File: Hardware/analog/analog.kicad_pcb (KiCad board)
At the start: 4 copper layers, 128 x 182 mm, 117 parts, among them J201 Würth 74651194R, J202 Würth 74651194R, J301 Conn_02x10_Odd_Even, J501 Conn_01x01, J502 Conn_01x01, M501 Fan_4pin, Q201 IXTH80N075L2, Q501 MMBT3904, U201 ADA4522-2, U202 LM431SC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

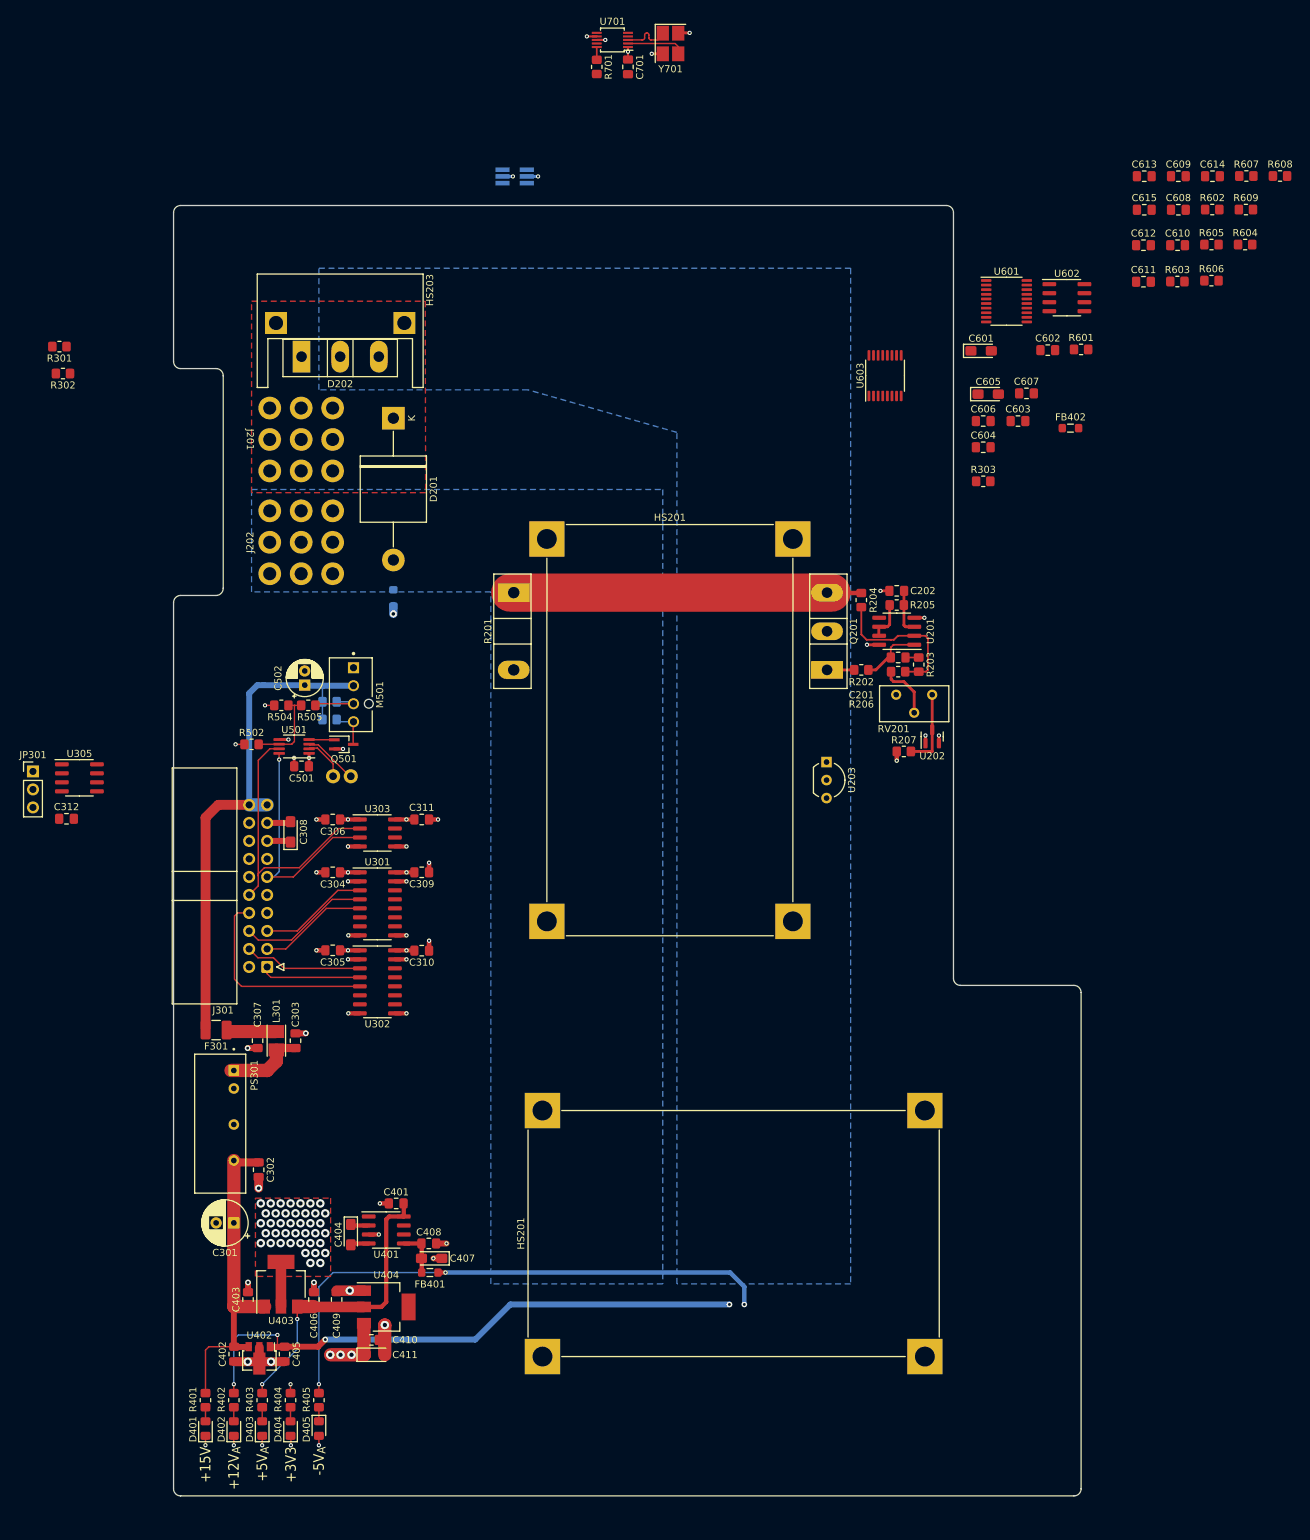
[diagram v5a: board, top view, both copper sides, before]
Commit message: Work on layout analog board
- Moved the heatsink to be horizontal near the bottom of the analog
  board, to give more open space for the analog circuitry away from the
  hot MOSFETs

- Minor tweak to bonus display (cutout for front panel jacks)
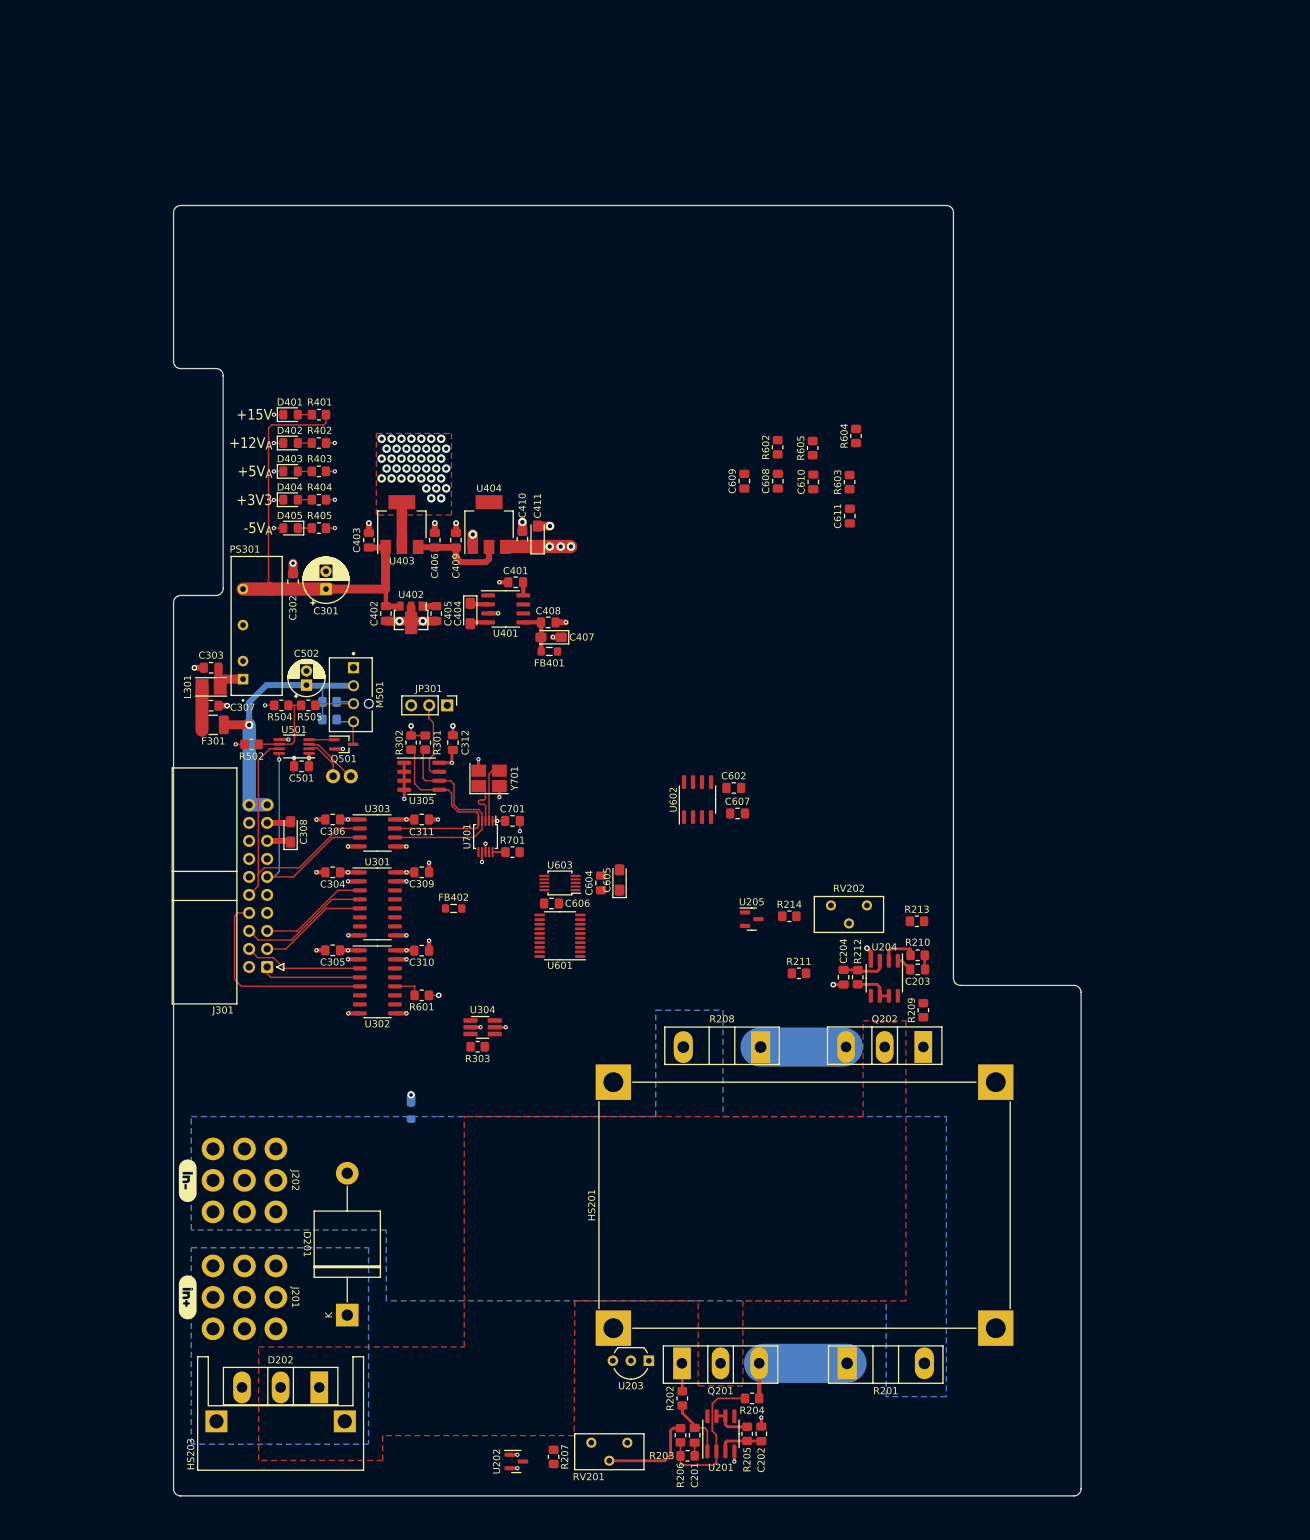
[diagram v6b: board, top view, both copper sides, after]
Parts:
- removed C601: 10µF, Capacitor_Tantalum_SMD:CP_EIA-3216-18_Kemet-A_Pad1.58x1.35mm_HandSolder
- removed C603, C612, C613, C614, C615: 100nF, Capacitor_SMD:C_0805_2012Metric_Pad1.18x1.45mm_HandSolder
- removed the HS201 at (70.0, 165.0)
- removed R606, R607, R608, R609: 1k, Resistor_SMD:R_0805_2012Metric_Pad1.20x1.40mm_HandSolder
- added C203: 1nF, Capacitor_SMD:C_0805_2012Metric_Pad1.18x1.45mm_HandSolder, F.Cu at (125.0, 127.8)
- added C204: 22nF, Capacitor_SMD:C_0805_2012Metric_Pad1.18x1.45mm_HandSolder, F.Cu at (114.5, 128.8)
- added Q202: IXTH80N075L2, Package_TO_SOT_THT:TO-247-3_Vertical, F.Cu at (125.8, 138.7)
- added R208: .05R, programmable-load:TO-247-2_Vertical, F.Cu at (102.8, 138.7)
- added R209: 100R, Resistor_SMD:R_0805_2012Metric_Pad1.20x1.40mm_HandSolder, F.Cu at (125.8, 133.5)
- added R210: 1k, Resistor_SMD:R_0805_2012Metric_Pad1.20x1.40mm_HandSolder, F.Cu at (125.0, 125.8)
- added R211: 1k, Resistor_SMD:R_0805_2012Metric_Pad1.20x1.40mm_HandSolder, F.Cu at (108.2, 128.3)
- added R212: 4k99, Resistor_SMD:R_0805_2012Metric_Pad1.20x1.40mm_HandSolder, F.Cu at (116.5, 128.8)
- added R213: 330k (?), Resistor_SMD:R_0805_2012Metric_Pad1.20x1.40mm_HandSolder, F.Cu at (124.8, 121.0)
- added R214: 1k, Resistor_SMD:R_0805_2012Metric_Pad1.20x1.40mm_HandSolder, F.Cu at (106.8, 120.2)
- added RV202: 10k, programmable-load:Potentiometer_Nidec_Copal_CT94EY, F.Cu at (117.8, 118.7)
- added U204: ADA4522-2, Package_SO:SOIC-8_3.9x4.9mm_P1.27mm, F.Cu at (120.2, 129.0)
- added U205: LM431SC, Package_TO_SOT_SMD:SOT-23, F.Cu at (101.5, 120.7)
- added kibuzzard-6280396F: G***, kibuzzard-6280396F, F.Cu at (22.0, 157.6)
- added kibuzzard-62803980: G***, kibuzzard-62803980, F.Cu at (22.0, 174.0)
- U304: moved to F.Cu
- U601: value MCP3564 -> MCP3562
- U603: value DAC8564 -> DAC8562; footprint Package_SO:TSSOP-16_4.4x5mm_P0.65mm -> Package_SO:MSOP-10_3x3mm_P0.5mm
- moved HS203 152.9 mm to (35.1, 190.4), turned to 90 degrees
- moved D202 145.4 mm to (40.5, 186.7), turned to 180 degrees
- moved D401 143.5 mm to (36.5, 49.5), turned to 0 degrees
- moved R401 139.9 mm to (40.5, 49.5), turned to 180 degrees
- moved D402 139.2 mm to (36.5, 53.5), turned to 0 degrees
- moved R402 135.5 mm to (40.5, 53.5), turned to 180 degrees
- moved D403 135.1 mm to (36.5, 57.5), turned to 0 degrees
- moved R403 131.2 mm to (40.5, 57.5), turned to 180 degrees
- moved D404 131.0 mm to (36.5, 61.5), turned to 0 degrees
- moved R601 130.2 mm to (55.0, 131.4)
- moved D405 127.1 mm to (36.5, 65.5), turned to 180 degrees
- moved R404 127.1 mm to (40.5, 61.5), turned to 180 degrees
- moved D201 126.7 mm to (44.5, 176.5), turned to 90 degrees
- moved R405 123.0 mm to (40.5, 65.5), turned to 180 degrees
- moved J201 121.3 mm to (30.0, 174.0), turned to 180 degrees
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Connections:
- RV201 pad 3: /MOSFET Load/VREF0 -> /MOSFET Load/VREF
- U601 pad 10: /Analog stuff/Sense_{2- -> unconnected-(U601-Pad10)
- U601 pad 11: /Analog stuff/Sense_{3+ -> unconnected-(U601-Pad11)
- U601 pad 12: /Analog stuff/Sense_{3- -> unconnected-(U601-Pad12)
- U601 pad 9: /Analog stuff/Sense_{2+ -> unconnected-(U601-Pad9)
- U603 pad 10: /Analog stuff/SPI_SCK -> /Analog stuff/VREF
- U603 pad 3: /Analog stuff/VREF -> GNDA
- U603 pad 4: +3V3A -> GND
- U603 pad 5: GNDA -> unconnected-(U603-Pad5)
- U603 pad 6: GNDA -> /Analog stuff/~{CS_DAC}
- U603 pad 7: /ISet_{2 -> /Analog stuff/SPI_SCK
- U603 pad 8: /ISet_{3 -> /Analog stuff/SPI_MOSI
- U603 pad 9: /Analog stuff/~{CS_DAC} -> +3V3A
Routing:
- net +12VA: track 196.3 -> 3.34 mm, vias 5 -> 1
- net -5VA: track 178.2 -> 1.25 mm, vias 4 -> 1
- net VBUS: track 75.2 -> 41.4 mm, vias 0 -> 1
- net /MOSFET Load/ISense0: track 50.2 -> 16.6 mm
- net /I2C_SCL: track 0.00 -> 30.8 mm
- net /I2C_SDA: track 0.00 -> 30.3 mm
- net +5VA: track 43.0 -> 19.6 mm, vias 2 -> 1
- net +15V: track 46.6 -> 65.4 mm
- net /MOSFET Load/ISense1: track 0.00 -> 11.8 mm
- net Net-(JP301-Pad2): track 0.00 -> 11.1 mm
- net Net-(R207-Pad1): track 11.0 -> 0.00 mm
- net GND: track 65.5 -> 74.8 mm, vias 73 -> 80
- net +3V3: track 22.6 -> 31.0 mm, vias 10 -> 13
- net Net-(C204-Pad1): track 0.00 -> 6.45 mm
- net Net-(R206-Pad1): track 7.99 -> 14.0 mm
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- added copper zone on F.Cu, net +VDC
- added copper zone on B.Cu, net /MOSFET Load/VBUS_IN
- removed copper zone on B.Cu, net +VDC
- removed copper zone on F.Cu, net /MOSFET Load/VBUS_IN

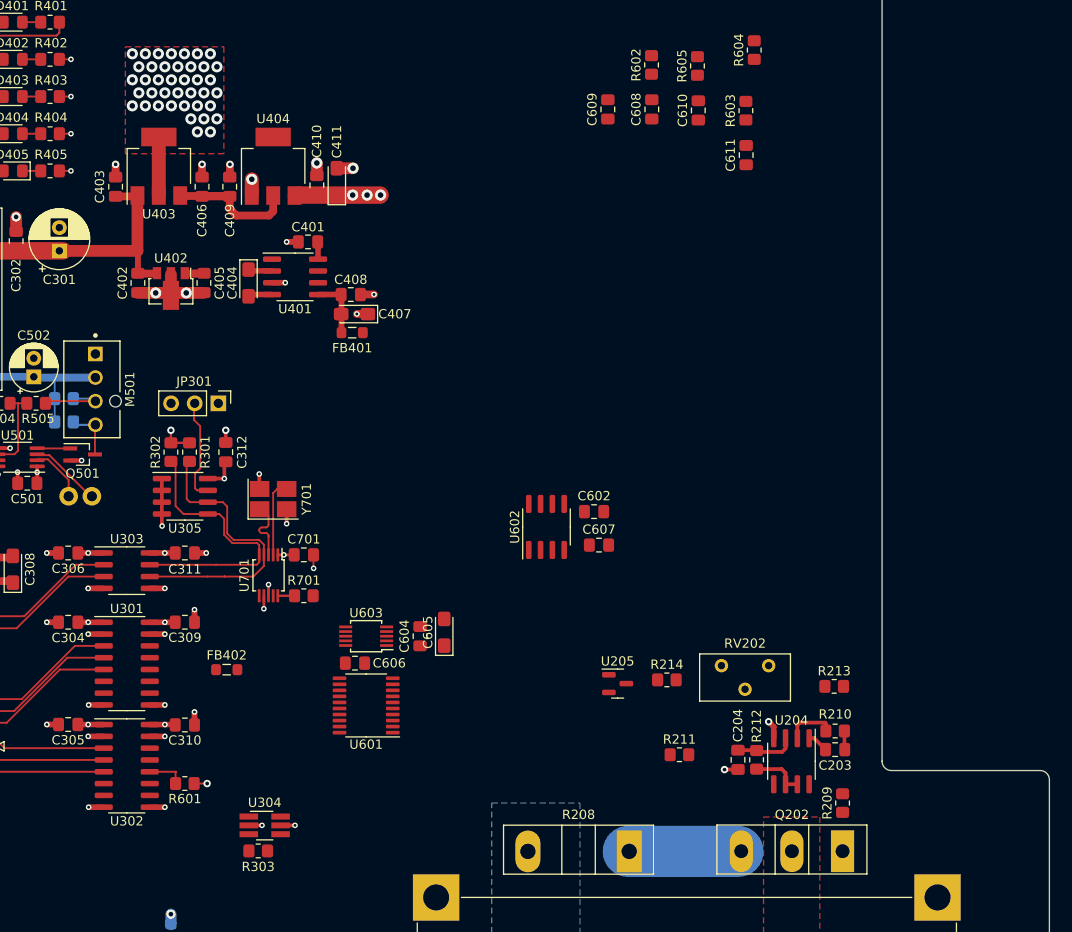
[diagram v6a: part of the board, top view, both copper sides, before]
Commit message: Start work on analog island
- This is the part with the ADC/DAC/reference which has its own analog
  ground and voltage, generated from +5V
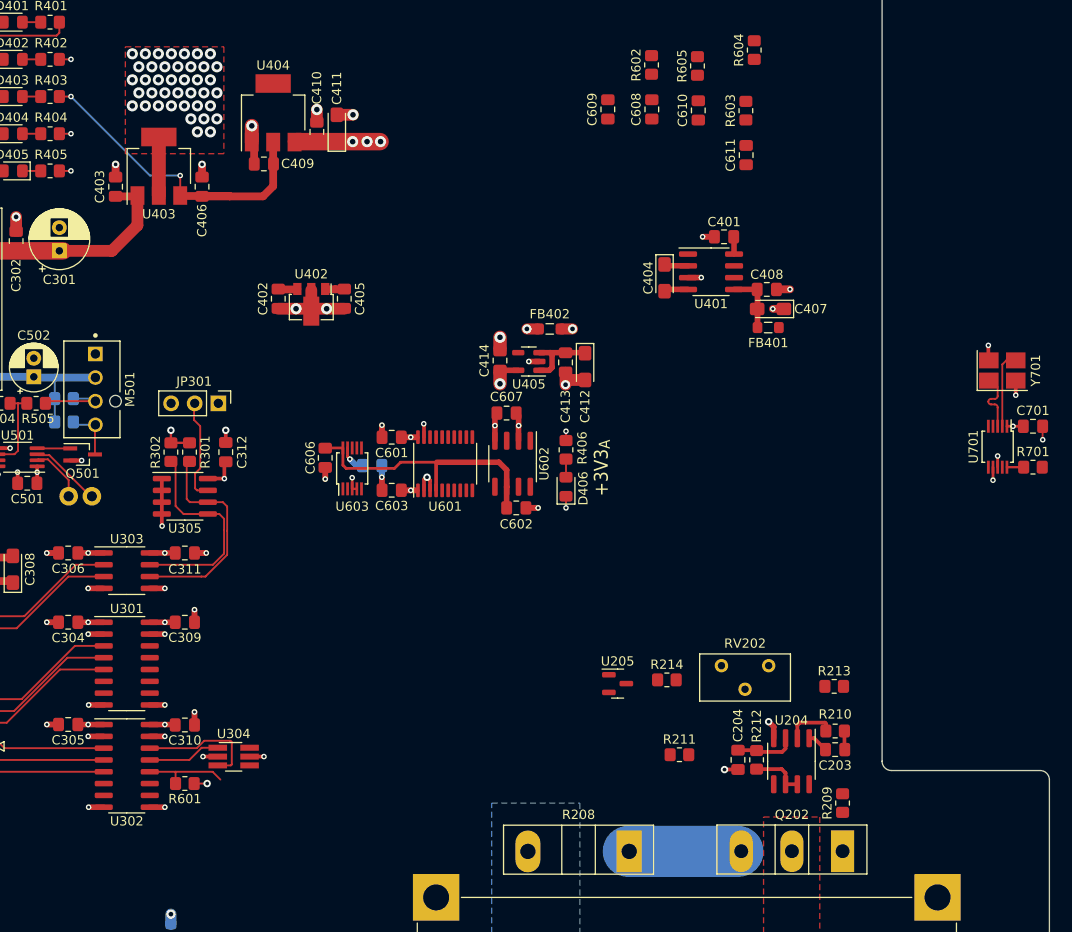
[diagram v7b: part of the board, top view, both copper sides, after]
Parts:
- removed C605: 10µF, Capacitor_Tantalum_SMD:CP_EIA-3216-18_Kemet-A_Pad1.58x1.35mm_HandSolder
- removed R303: 10k, Resistor_SMD:R_0805_2012Metric_Pad1.20x1.40mm_HandSolder
- added C412: 10µF, Capacitor_Tantalum_SMD:CP_EIA-3216-18_Kemet-A_Pad1.58x1.35mm_HandSolder, F.Cu at (98.0, 86.5)
- added C413: 4.7µF, Capacitor_SMD:C_0805_2012Metric_Pad1.18x1.45mm_HandSolder, F.Cu at (96.0, 86.1)
- added C414: 4.7µF, Capacitor_SMD:C_0805_2012Metric_Pad1.18x1.45mm_HandSolder, F.Cu at (88.9, 85.9)
- added C601: 100nF, Capacitor_SMD:C_0805_2012Metric_Pad1.18x1.45mm_HandSolder, F.Cu at (77.2, 94.2)
- added C603: 100nF, Capacitor_SMD:C_0805_2012Metric_Pad1.18x1.45mm_HandSolder, F.Cu at (77.2, 99.8)
- added D406: Green, LED_SMD:LED_0805_2012Metric_Pad1.15x1.40mm_HandSolder, F.Cu at (96.0, 99.5)
- added R406: 1k, Resistor_SMD:R_0805_2012Metric_Pad1.20x1.40mm_HandSolder, F.Cu at (96.0, 95.5)
- added U405: LP5907MFX-3.3, Package_TO_SOT_SMD:SOT-23-5, F.Cu at (92.0, 86.0)
- C604: moved to B.Cu
- moved U701 79.6 mm to (142.4, 95.2)
- moved Y701 79.6 mm to (142.9, 87.0)
- moved C701 79.6 mm to (146.2, 93.0)
- moved R701 79.6 mm to (146.2, 97.4)
- moved FB402 50.5 mm to (94.2, 82.5), turned to 180 degrees
- moved C401 44.8 mm to (113.0, 72.6)
- moved C407 44.8 mm to (118.0, 80.3)
- moved C408 44.8 mm to (117.6, 78.2)
- moved FB401 44.8 mm to (117.8, 82.3)
- moved U401 44.8 mm to (111.6, 76.3)
- moved C404 44.8 mm to (106.6, 77.0)
- moved U601 27.4 mm to (83.0, 97.0), turned to 90 degrees
- moved C606 22.3 mm to (70.1, 96.4), turned to -90 degrees
- moved C604 19.1 mm to (75.2, 97.2), turned to 0 degrees
- moved U603 18.1 mm to (73.0, 97.5), turned to 90 degrees
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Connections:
- U304 pad 4: /Analog stuff/~{CS_DAC} -> /Analog stuff/~{CS_ADC}
- U304 pad 6: /Analog stuff/~{CS_ADC} -> /Analog stuff/~{CS_DAC}
- U603 pad 4: GND -> GNDA
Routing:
- net /Analog stuff/VREF: track 0.00 -> 29.2 mm
- net +5VA: track 19.6 -> 46.8 mm, vias 1 -> 2
- net GNDA: track 0.00 -> 17.7 mm, vias 0 -> 10
- net /External Interface/~{SEL_EN}: track 0.00 -> 13.2 mm
- net +3V3A: track 0.00 -> 11.6 mm, vias 0 -> 5
- net /I2C_SCL: track 30.8 -> 22.9 mm
- net /External Interface/SEL_0: track 0.00 -> 7.86 mm
- net /I2C_SDA: track 30.3 -> 22.8 mm
- net GND: track 74.8 -> 81.7 mm, vias 80 -> 83
- net /Analog stuff/~{IRQ}: track 4.13 -> 9.22 mm
- net +15V: track 65.4 -> 61.4 mm
- net Net-(D406-Pad2): track 0.00 -> 1.95 mm
- net +3V3: track 31.0 -> 32.6 mm, vias 13 -> 14
- added copper zone on In2.Cu, net +3V3A
- added copper zone on In1.Cu, net GNDA
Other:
- board text added: "+3V3_{A}"
